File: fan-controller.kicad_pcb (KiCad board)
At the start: 2 copper layers, 34.5 x 20 mm, 24 parts, among them J1 PWR, J2 PTC, J3 FAN, J4 Conn_ARM_SWD_TagConnect_TC203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, Q1 AO3401A, Q2 MMBT5401, Q3 MMBT5551, Q4 MMBT5551, U1 L78L05, U2 PY32F002A

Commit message: Fix some bugs & add PWM jumper
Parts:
- added JP1: PWM_MODE, Jumper:SolderJumper-2_P1.3mm_Open_TrianglePad1.0x1.5mm, B.Cu at (122.0, 63.0)
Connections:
- net +3.3V renamed +5V
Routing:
- net Net-(D1-K): track 12.5 -> 15.0 mm, vias 0 -> 1
- net /FAN_OUT: track 27.3 -> 29.6 mm, vias 0 -> 1
- net VPP: track 40.7 -> 38.6 mm
- net /SW: track 3.30 -> 2.64 mm
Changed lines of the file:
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@@
   )
   (net 0 "")
-  (net 1 "+3.3V")
+  (net 1 "+5V")
   (net 2 "GND")
   (net 3 "VPP")
@@
       (stroke (width 0.1) (type solid)) (layer "F.Fab"))
     (pad "1" smd roundrect (at -1.4625 0) (size 1.125 1.75) (layers "F.Cu" "F.Paste" "F.Mask") (roundrect_rratio 0.222222)
-      (net 1 "+3.3V") (pintype "passive"))
+      (net 1 "+5V") (pintype "passive"))
     (pad "2" smd roundrect (at 1.4625 0) (size 1.125 1.75) (layers "F.Cu" "F.Paste" "F.Mask") (roundrect_rratio 0.222222)
       (net 2 "GND") (pintype "passive"))
@@
     (descr "SOT, 3 Pin (https://www.jedec.org/system/files/docs/to-236h.pdf variant AB), generated with kicad-footprint-generator ipc_gullwing_generator.py")
     (tags "SOT TO_SOT_SMD")
+    (property "LCSC" "C2145")
     (property "Sheetfile" "fan-controller.kicad_sch")
     (property "Sheetname" "")
@@
     (pad "" np_thru_hole circle (at 2.54 1.016 180) (size 0.9906 0.9906) (drill 0.9906) (layers "*.Cu" "*.Mask"))
     (pad "1" connect circle (at -1.27 0.635 180) (size 0.7874 0.7874) (layers "F.Cu" "F.Mask")
-      (net 1 "+3.3V") (pinfunction "VCC") (pintype "power_in"))
+      (net 1 "+5V") (pinfunction "VCC") (pintype "power_in"))
     (pad "2" connect circle (at -1.27 -0.635 180) (size 0.7874 0.7874) (layers "F.Cu" "F.Mask")
       (net 5 "/SWDIO") (pinfunction "SWDIO") (pintype "bidirectional"))
@@
       (net 8 "/~{RST}") (pintype "passive"))
     (pad "2" smd roundrect (at 0.51 0) (size 0.54 0.64) (layers "F.Cu" "F.Paste" "F.Mask") (roundrect_rratio 0.25)
-      (net 1 "+3.3V") (pintype "passive"))
+      (net 1 "+5V") (pintype "passive"))
     (model "${KICAD6_3DMODEL_DIR}/Resistor_SMD.3dshapes/R_0402_1005Metric.wrl"
       (offset (xyz 0 0 0))
@@
     (descr "SOT, 3 Pin (https://www.jedec.org/system/files/docs/to-236h.pdf variant AB), generated with kicad-footprint-generator ipc_gullwing_generator.py")
     (tags "SOT TO_SOT_SMD")
+    (property "LCSC" "C2145")
     (property "Sheetfile" "fan-controller.kicad_sch")
     (property "Sheetname" "")
@@
       (stroke (width 0.1) (type solid)) (layer "F.Fab"))
     (pad "1" smd rect (at -1.65 -1.5 180) (size 1.3 0.9) (layers "F.Cu" "F.Paste" "F.Mask")
-      (net 1 "+3.3V") (pinfunction "OUT") (pintype "power_out"))
+      (net 1 "+5V") (pinfunction "OUT") (pintype "power_out"))
     (pad "2" smd custom (at -1.5625 0 180) (size 1.475 0.9) (layers "F.Cu" "F.Paste" "F.Mask")
       (net 2 "GND") (pinfunction "GND") (pintype "power_in") (zone_connect 2) (thermal_bridge_angle 45)
@@
     (descr "SOT, 3 Pin (https://www.jedec.org/system/files/docs/to-236h.pdf variant AB), generated with kicad-footprint-generator ipc_gullwing_generator.py")
     (tags "SOT TO_SOT_SMD")
+    (property "LCSC" "C8326")
     (property "Sheetfile" "fan-controller.kicad_sch")
     (property "Sheetname" "")
@@
       (stroke (width 0.1) (type solid)) (layer "F.Fab"))
     (pad "1" smd roundrect (at -2.475 -1.905) (size 1.95 0.6) (layers "F.Cu" "F.Paste" "F.Mask") (roundrect_rratio 0.25)
-      (net 1 "+3.3V") (pinfunction "VCC") (pintype "power_in"))
+      (net 1 "+5V") (pinfunction "VCC") (pintype "power_in"))
     (pad "2" smd roundrect (at -2.475 -0.635) (size 1.95 0.6) (layers "F.Cu" "F.Paste" "F.Mask") (roundrect_rratio 0.25)
       (net 11 "/FAN_SENSE") (pinfunction "PA4/PA10") (pintype "bidirectional"))
@@
       (stroke (width 0.1) (type solid)) (layer "F.Fab"))
     (pad "1" thru_hole rect (at 0 0) (size 1.7 1.7) (drill 1) (layers "*.Cu" "*.Mask")
-      (net 1 "+3.3V") (pinfunction "Pin_1") (pintype "passive"))
+      (net 1 "+5V") (pinfunction "Pin_1") (pintype "passive"))
     (pad "2" thru_hole oval (at 0 2.54) (size 1.7 1.7) (drill 1) (layers "*.Cu" "*.Mask")
       (net 4 "/TEMP_SENSE") (pinfunction "Pin_2") (pintype "passive"))
@@
       (rotate (xyz 0 0 0))
     )
+  )
+  (footprint "Jumper:SolderJumper-2_P1.3mm_Open_TrianglePad1.0x1.5mm" (layer "B.Cu")
+    (at 122 63)
+    (descr "SMD Solder Jumper, 1x1.5mm Triangular Pads, 0.3mm gap, open")
+    (tags "solder jumper open")
+    (property "Sheetfile" "fan-controller.kicad_sch")
+    (property "Sheetname" "")
+    (property "ki_description" "Solder Jumper, 2-pole, open")
+    (property "ki_keywords" "solder jumper SPST")
+    (attr exclude_from_pos_files)
+    (fp_text reference "JP1" (at 0 1.8) (layer "B.SilkS")
+        (effects (font (size 1 1) (thickness 0.15)) (justify mirror))
+    )
+    (fp_text value "PWM_MODE" (at 0 -1.9) (layer "B.Fab")
+        (effects (font (size 1 1) (thickness 0.15)) (justify mirror))
+    )
+    (fp_line (start -1.4 -1) (end -1.4 1)
+      (stroke (width 0.12) (type solid)) (layer "B.SilkS"))
+    (fp_line (start -1.4 1) (end 1.4 1)
+      (stroke (width 0.12) (type solid)) (layer "B.SilkS"))
+    (fp_line (start 1.4 -1) (end -1.4 -1)
+      (stroke (width 0.12) (type solid)) (layer "B.SilkS"))
+    (fp_line (start 1.4 1) (end 1.4 -1)
+      (stroke (width 0.12) (type solid)) (layer "B.SilkS"))
+    (fp_line (start -1.65 1.25) (end -1.65 -1.25)
+      (stroke (width 0.05) (type solid)) (layer "B.CrtYd"))
+    (fp_line (start -1.65 1.25) (end 1.65 1.25)
+      (stroke (width 0.05) (type solid)) (layer "B.CrtYd"))
+    (fp_line (start 1.65 -1.25) (end -1.65 -1.25)
+      (stroke (width 0.05) (type solid)) (layer "B.CrtYd"))
+    (fp_line (start 1.65 -1.25) (end 1.65 1.25)
+      (stroke (width 0.05) (type solid)) (layer "B.CrtYd"))
+    (pad "1" smd custom (at -0.725 0) (size 0.3 0.3) (layers "B.Cu" "B.Mask")
+      (net 9 "Net-(D1-K)") (pinfunction "A") (pintype "passive") (zone_connect 2) (thermal_bridge_angle 45)
+      (options (clearance outline) (anchor rect))
+      (primitives
+        (gr_poly
+          (pts
+            (xy 1 0)
+            (xy 0.5 -0.75)
+            (xy -0.5 -0.75)
+            (xy -0.5 0.75)
+            (xy 0.5 0.75)
+          )
+          (width 0) (fill yes))
+      ))
+    (pad "2" smd custom (at 0.725 0) (size 0.3 0.3) (layers "B.Cu" "B.Mask")
+      (net 10 "/FAN_OUT") (pinfunction "B") (pintype "passive") (zone_connect 2) (thermal_bridge_angle 45)
+      (options (clearance outline) (anchor rect))
+      (primitives
+        (gr_poly
+          (pts
+            (xy 0.5 -0.75)
+            (xy -0.65 -0.75)
+            (xy -0.15 0)
+            (xy -0.65 0.75)
+            (xy 0.5 0.75)
+          )
+          (width 0) (fill yes))
+      ))
   )
   (gr_rect (start 98.5 52) (end 133 72)
@@
   (via (at 122.5 66.5) (size 0.8) (drill 0.4) (layers "F.Cu" "B.Cu") (net 2))
   (segment (start 119 53) (end 121.5 53) (width 1) (layer "F.Cu") (net 3))
-  (segment (start 109.238 53.3) (end 107.15 53.3) (width 0.25) (layer "F.Cu") (net 3))
   (segment (start 121.45 58.9375) (end 121.45 56.05) (width 0.5) (layer "F.Cu") (net 3))
   (segment (start 121.45 56.05) (end 121.5 56) (width 0.5) (layer "F.Cu") (net 3))
@@
   (segment (start 104.0897 66.3403) (end 104.0897 70.37649) (width 0.25) (layer "F.Cu") (net 6))
   (segment (start 106.1137 70.8863) (end 107.5 69.5) (width 0.25) (layer "F.Cu") (net 6))
-  (segment (start 113.475 59.365) (end 114.135 59.365) (width 0.25) (layer "F.Cu") (net 7))
   (segment (start 114.135 59.365) (end 116 57.5) (width 0.25) (layer "F.Cu") (net 7))
   (segment (start 113.0895 60.635) (end 110.7245 63) (width 0.25) (layer "F.Cu") (net 8))
@@
   (segment (start 110.7245 63) (end 109.2755 63) (width 0.25) (layer "B.Cu") (net 8))
   (segment (start 120.5 57.0625) (end 120.5 62.5) (width 0.5) (layer "F.Cu") (net 9))
+  (segment (start 120.5 64.444365) (end 120.5 62.5) (width 1) (layer "F.Cu") (net 9))
   (segment (start 118 68.5) (end 118 66.944365) (width 1) (layer "F.Cu") (net 9))
-  (segment (start 120.5 64.444365) (end 120.5 62.5) (width 1) (layer "F.Cu") (net 9))
   (segment (start 118 66.944365) (end 120.5 64.444365) (width 1) (layer "F.Cu") (net 9))
+  (via (at 119.972182 64.972182) (size 0.8) (drill 0.4) (layers "F.Cu" "B.Cu") (net 9))
+  (segment (start 121.275 63) (end 121.275 63.197182) (width 0.25) (layer "B.Cu") (net 9))
+  (segment (start 121.275 63.197182) (end 119.972182 64.5) (width 0.25) (layer "B.Cu") (net 9))
+  (segment (start 119.972182 64.972182) (end 119.972182 64.5) (width 0.25) (layer "B.Cu") (net 9))
+  (segment (start 123.5 62.5) (end 123.5 65) (width 1) (layer "F.Cu") (net 10))
   (segment (start 123.5 65) (end 124 65.5) (width 1) (layer "F.Cu") (net 10))
-  (segment (start 123.5 62.5) (end 123.5 65) (width 1) (layer "F.Cu") (net 10))
   (segment (start 124 65.5) (end 124 69) (width 0.5) (layer "F.Cu") (net 10))
   (segment (start 112.5 66.5) (end 111.5 67.5) (width 0.25) (layer "F.Cu") (net 10))
@@
   (segment (start 112.5 66.01) (end 112.5 66.5) (width 0.25) (layer "F.Cu") (net 10))
   (segment (start 111.5 67.5) (end 111.5 68.5) (width 0.25) (layer "F.Cu") (net 10))
+  (via (at 123.5 65) (size 0.8) (drill 0.4) (layers "F.Cu" "B.Cu") (net 10))
+  (segment (start 122.725 63) (end 122.725 63.225) (width 0.25) (layer "B.Cu") (net 10))
+  (segment (start 123.5 64) (end 123.5 65) (width 0.25) (layer "B.Cu") (net 10))
+  (segment (start 122.725 63.225) (end 123.5 64) (width 0.25) (layer "B.Cu") (net 10))
   (segment (start 114.775 62.699695) (end 112.5 64.974695) (width 0.25) (layer "F.Cu") (net 11))
   (segment (start 112.463249 60) (end 114.486751 60) (width 0.25) (layer "F.Cu") (net 11))

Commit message: Simplify circuit
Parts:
- removed JP1: PWM_MODE, Jumper:SolderJumper-2_P1.3mm_Open_TrianglePad1.0x1.5mm
- removed Q1: AO3401A, Package_TO_SOT_SMD:SOT-23
- removed Q2: MMBT5401, Package_TO_SOT_SMD:SOT-23
- removed Q3, Q4: MMBT5551, Package_TO_SOT_SMD:SOT-23
- removed R7: 22k, Resistor_SMD:R_0402_1005Metric
- added Q5: AO3400A, Package_TO_SOT_SMD:SOT-23, F.Cu at (117.0, 62.0)
- added R5: 100, Resistor_SMD:R_0402_1005Metric, F.Cu at (116.0, 59.5)
- R2: value 22k -> 100k
- R3: value 100k -> 22k
- moved D1 7.81 mm to (121.0, 62.5), turned to -90 degrees
- moved L1 7.50 mm to (117.5, 56.5)
- moved C3 6.18 mm to (116.5, 67.5)
- moved C4 6.18 mm to (116.5, 65.0)
- moved J1 2.25 mm to (125.8, 57.0)
- moved J3 2.25 mm to (125.8, 65.0)
- moved kibuzzard-1 2.25 mm to (129.0, 58.2)
- moved kibuzzard-3 2.25 mm to (129.0, 66.2)
- moved R2 1.12 mm to (112.5, 66.0), turned to 180 degrees
- moved J4 0.56 mm to (107.5, 68.4)
- moved R4 0.56 mm to (108.2, 65.8)
- moved R3 0.50 mm to (112.5, 65.0), turned to 180 degrees
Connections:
- C3 pad 1: /FAN_OUT -> /FAN_OUT-
- C4 pad 1: /FAN_OUT -> /FAN_OUT-
- D1 pad 1: Net-(D1-K) -> /FAN_OUT-
- D1 pad 2: GND -> Net-(D1-A)
- J3 pad 1: /FAN_OUT -> VPP
- J3 pad 2: GND -> /FAN_OUT-
- J4 pad 6: /~{RST} -> unconnected-(J4-SWO-Pad6)
- L1 pad 1: Net-(D1-K) -> Net-(D1-A)
- L1 pad 2: /FAN_OUT -> /FAN_OUT-
- R2 pad 1: /FAN_SENSE -> /FAN_OUT-
- R2 pad 2: GND -> Net-(U2-PA4/PA10)
- R3 pad 1: /FAN_OUT -> GND
- R3 pad 2: /FAN_SENSE -> Net-(U2-PA4/PA10)
- U2 pad 2: /FAN_SENSE -> Net-(U2-PA4/PA10)
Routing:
- net /FAN_OUT-: track 0.00 -> 30.4 mm
- net /FAN_OUT: track 29.6 -> 0.00 mm, vias 1 -> 0
- net GND: track 23.2 -> 47.5 mm, vias 17 -> 16
- net Net-(D1-K): track 15.0 -> 0.00 mm, vias 1 -> 0
- net /FAN_SENSE: track 13.3 -> 0.00 mm
- net Net-(Q2-B): track 12.9 -> 0.00 mm
- net Net-(D1-A): track 0.00 -> 9.39 mm
- net Net-(U2-PA4/PA10): track 0.00 -> 8.65 mm, vias 0 -> 2
- net VPP: track 38.6 -> 31.7 mm
- net Net-(Q1-G): track 5.33 -> 0.00 mm
- net /SWCLK: track 14.5 -> 10.2 mm, vias 0 -> 2
- net /~{RST}: track 12.5 -> 10.1 mm
- net Net-(Q5-G): track 0.00 -> 1.72 mm
- net /SWDIO: track 12.2 -> 11.4 mm
- net +5V: track 23.1 -> 22.6 mm
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- added copper zone on F.Cu, net (none)
- removed copper zone on F.Cu, net GND
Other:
- board size 34.5 x 20 mm -> 32 x 20 mm
- board text added: "flaviutamas.com/p/fan-temp 5-24V Fan Temp Controller Ifan≤300mA"
- board text removed: "flaviutamas.com/p/dc-fan-temp 5-24V Fan Temp Controller Ifan≤250mA"

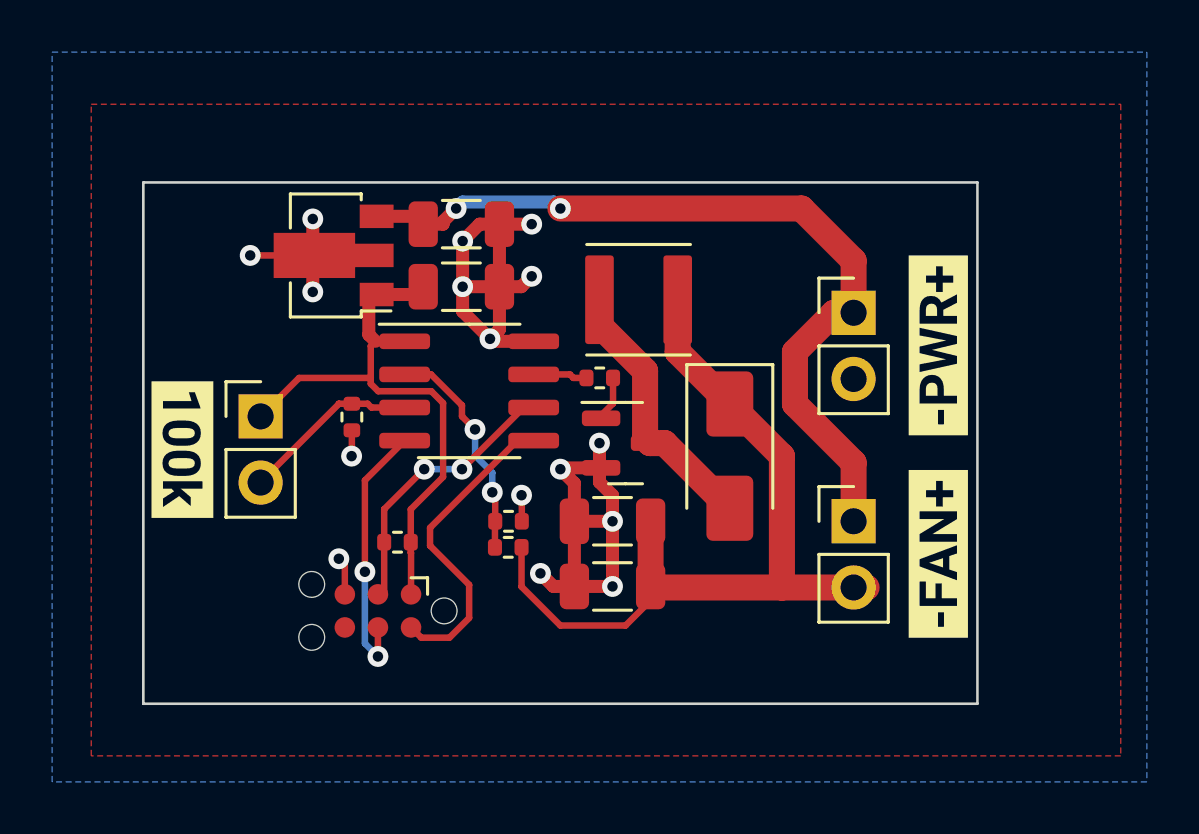
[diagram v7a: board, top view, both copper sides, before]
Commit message: Fix dumb errors (wrong part #)
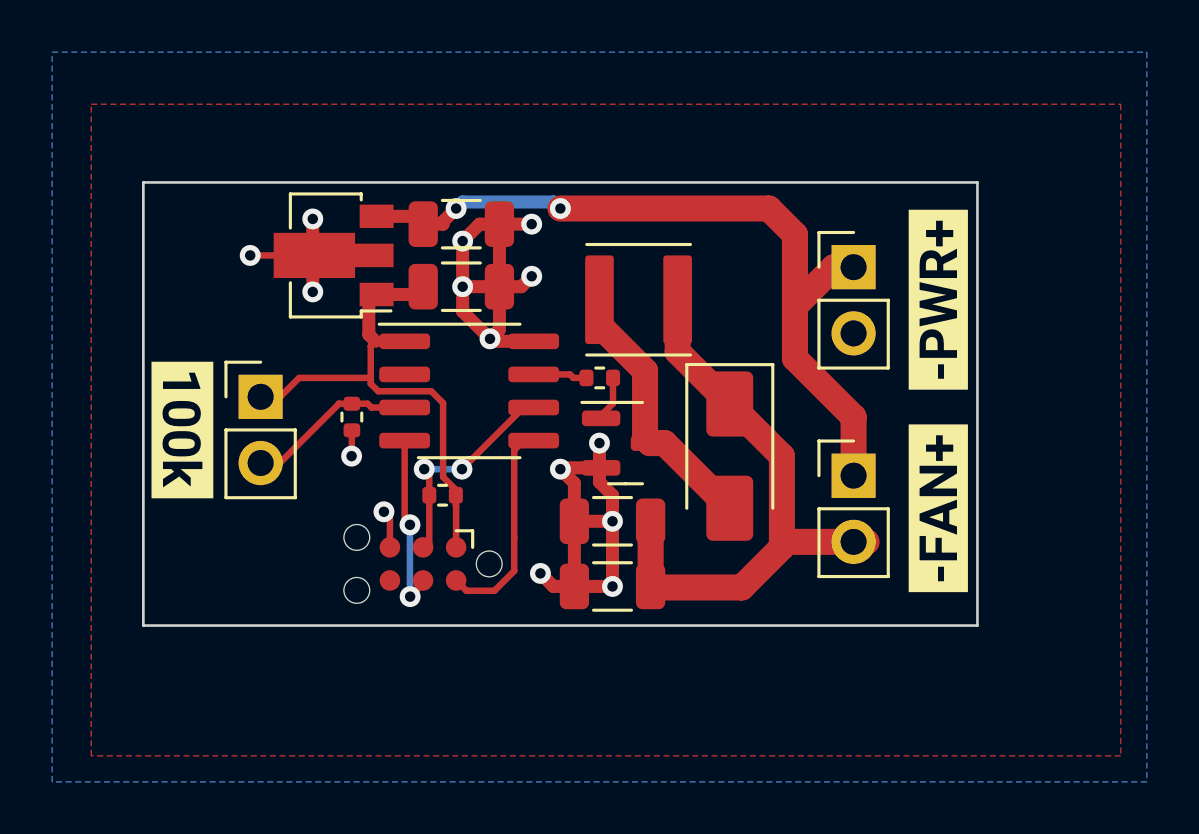
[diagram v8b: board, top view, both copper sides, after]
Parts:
- removed R2: 100k, Resistor_SMD:R_0402_1005Metric
- removed R3: 22k, Resistor_SMD:R_0402_1005Metric
- moved J4 2.50 mm to (109.2, 66.6)
- moved R4 2.50 mm to (110.0, 64.0)
- moved J1 1.75 mm to (125.8, 55.2)
- moved J3 1.75 mm to (125.8, 63.2)
- moved kibuzzard-1 1.75 mm to (129.0, 56.5)
- moved kibuzzard-3 1.75 mm to (129.0, 64.5)
- moved J2 0.75 mm to (103.0, 60.2)
- moved kibuzzard-2 0.75 mm to (100.0, 61.5)
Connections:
- U2 pad 2: Net-(U2-PA4/PA10) -> unconnected-(U2-PA4/PA10-Pad2)
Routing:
- net Net-(U2-PA4/PA10): track 8.65 -> 0.00 mm, vias 2 -> 0
- net /FAN_OUT-: track 30.4 -> 22.0 mm
- net /SWDIO: track 11.4 -> 7.72 mm
- net /SWCLK: track 10.2 -> 6.89 mm
- net +5V: track 22.6 -> 20.1 mm
- net /~{RST}: track 10.1 -> 7.77 mm
- net VPP: track 31.7 -> 29.7 mm
- net GND: track 47.5 -> 46.5 mm, vias 16 -> 15
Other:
- board size 32 x 20 mm -> 32 x 17 mm
